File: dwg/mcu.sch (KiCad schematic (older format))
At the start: 3 parts

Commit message: updating board -- no DRC errors
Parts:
- added C17, C22, C23, C24, C25, C26, C27, C31: 0.1uF, Capacitors_SMD:C_0805_HandSoldering, symbol C_Small
- added C18, C20: 2.2uF, Capacitors_SMD:C_0805_HandSoldering, symbol C_Small
- added C19: 10uF, Capacitors_SMD:C_0805_HandSoldering, symbol C_Small
- added C28, C30: 20pF, Capacitors_SMD:C_0603_HandSoldering, symbol C_Small
- added C29: 1uF, Capacitors_SMD:C_0805_HandSoldering, symbol C_Small
- added J13: CONN_02X05, Connectors:IDC_Header_Straight_10pins, symbol CONN_02X05
- added R18, R19, R21: 10k, Resistors_SMD:R_0805_HandSoldering, symbol R_Small
- added R20: 300, Resistors_SMD:R_0603_HandSoldering, symbol R_Small
- added Y1: 8MHz, Crystals:Crystal_SMD_Abracon_ABM3-2pin_5.0x3.2mm_HandSoldering, symbol Crystal_Small
- SW1: renamed from SW?; value SW_PUSH -> TL3342; footprint (none) -> Buttons_Switches_SMD:SW_SPST_TL3342
- U3: renamed from U?; footprint LQFP100 -> Housings_QFP:LQFP-100_14x14mm_Pitch0.5mm
- gave numbers to parts that had none: 1
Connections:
- net CS_IRQ: now also U3.96 (CAN1_TX/DAC_EXTI9/DCMI_D7/I2C1_SDA/I2S2_WS/SDIO_D5/SPI2_NSS/TIM11_CH1/TIM4_CH4/PB9); no longer U3.1 (PE2/ETH_TXD3/FSMC_A23/SYS_TRACECLK)
- net GND: now also C21.2, U3.10 (VSS), U3.20 (VSSA), U3.27 (VSS), U3.74 (VSS), U3.99 (VSS), C17.2, C18.2, C19.2, C20.2, C22.2, C23.2, C24.2, C25.2, C26.2, C27.2, C29.2, C31.2, J13.3 (P3), J13.5 (P5), J13.9 (P9), R18.2, R19.2, R21.1; no longer C21.1
- net HAL_1: now also U3.78 (DCMI_D8/I2S3_CK/SDIO_D2/SPI3_SCK/UART4_TX/USART3_TX/PC10); no longer U3.5 (PE6/DCMI_D7/FSMC_A22/SYS_TRACED3/TIM9_CH2)
- net HAL_2: now also U3.82 (PD1/CAN1_TX/FSMC_D3/FSMC_DA3); no longer U3.3 (PE4/DCMI_D4/FSMC_A20/SYS_TRACED1)
- net VCC: now reaches U3.100 (VDD)
- net VCC: now also U3.11 (VDD), U3.19 (VDD), U3.28 (VDD), U3.50 (VDD), U3.6 (VBAT), U3.75 (VDD), C17.1, C19.1, C22.1, C23.1, C24.1, C25.1, C26.1, C27.1, J13.1 (P1)
- net OSC_IN: now reaches U3.12 (PH0/RCC_OSC_IN)
- net OSC_IN: now also C28.1, Y1.1
- net OSC_OUT: now reaches U3.13 (PH1/RCC_OSC_OUT)
- net OSC_OUT: now also R20.1
- net NRST: now reaches SW1.2, U3.14 (NRST)
- net NRST: now also C21.1, J13.10 (P10); no longer C21.2
- net VDDA: now reaches U3.21 (VREF+)
- net VDDA: now also U3.22 (VDDA), C29.1, C31.1
- net BOOT1: now reaches U3.37 (BOOT1/PB2)
- net BOOT1: now also R19.1
- net VCAP_1: now reaches U3.49 (VCAP_1)
- net VCAP_1: now also C20.1
- net JTMS/SWDIO: now reaches U3.72 (SYS_JTMS-SWDIO/PA13)
- net JTMS/SWDIO: now also J13.2 (P2)
- net VCAP_2: now reaches U3.73 (VCAP_2)
- net VCAP_2: now also C18.1
- net JTCK/SWCLK: now reaches U3.76 (SYS_JTCK-SWCLK/PA14)
- net JTCK/SWCLK: now also J13.4 (P4)
- net JTDI: now reaches U3.77 (ADC1_EXTI15/ADC2_EXTI15/ADC3_EXTI15/I2S3_WS/SPI1_NSS/SPI3_NSS/SYS_JTDI/TIM2_CH1/TIM2_ETR/PA15)
- net JTDI: now also J13.8 (P8)
- net JTDO/SWO: now reaches U3.89 (I2S3_CK/SPI1_SCK/SPI3_SCK/SYS_JTDO-SWO/TIM2_CH2/PB3)
- net JTDO/SWO: now also J13.6 (P6)
- net BOOT0: now reaches U3.94 (BOOT0)
- net BOOT0: now also R18.1
- new net: J13.7 (P7), R21.2
- new net: C30.1, R20.2, Y1.2
- new net: C28.2, C30.2
- no-connect marks 0 -> 53
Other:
- moved on the sheet: C21, SW1, U3

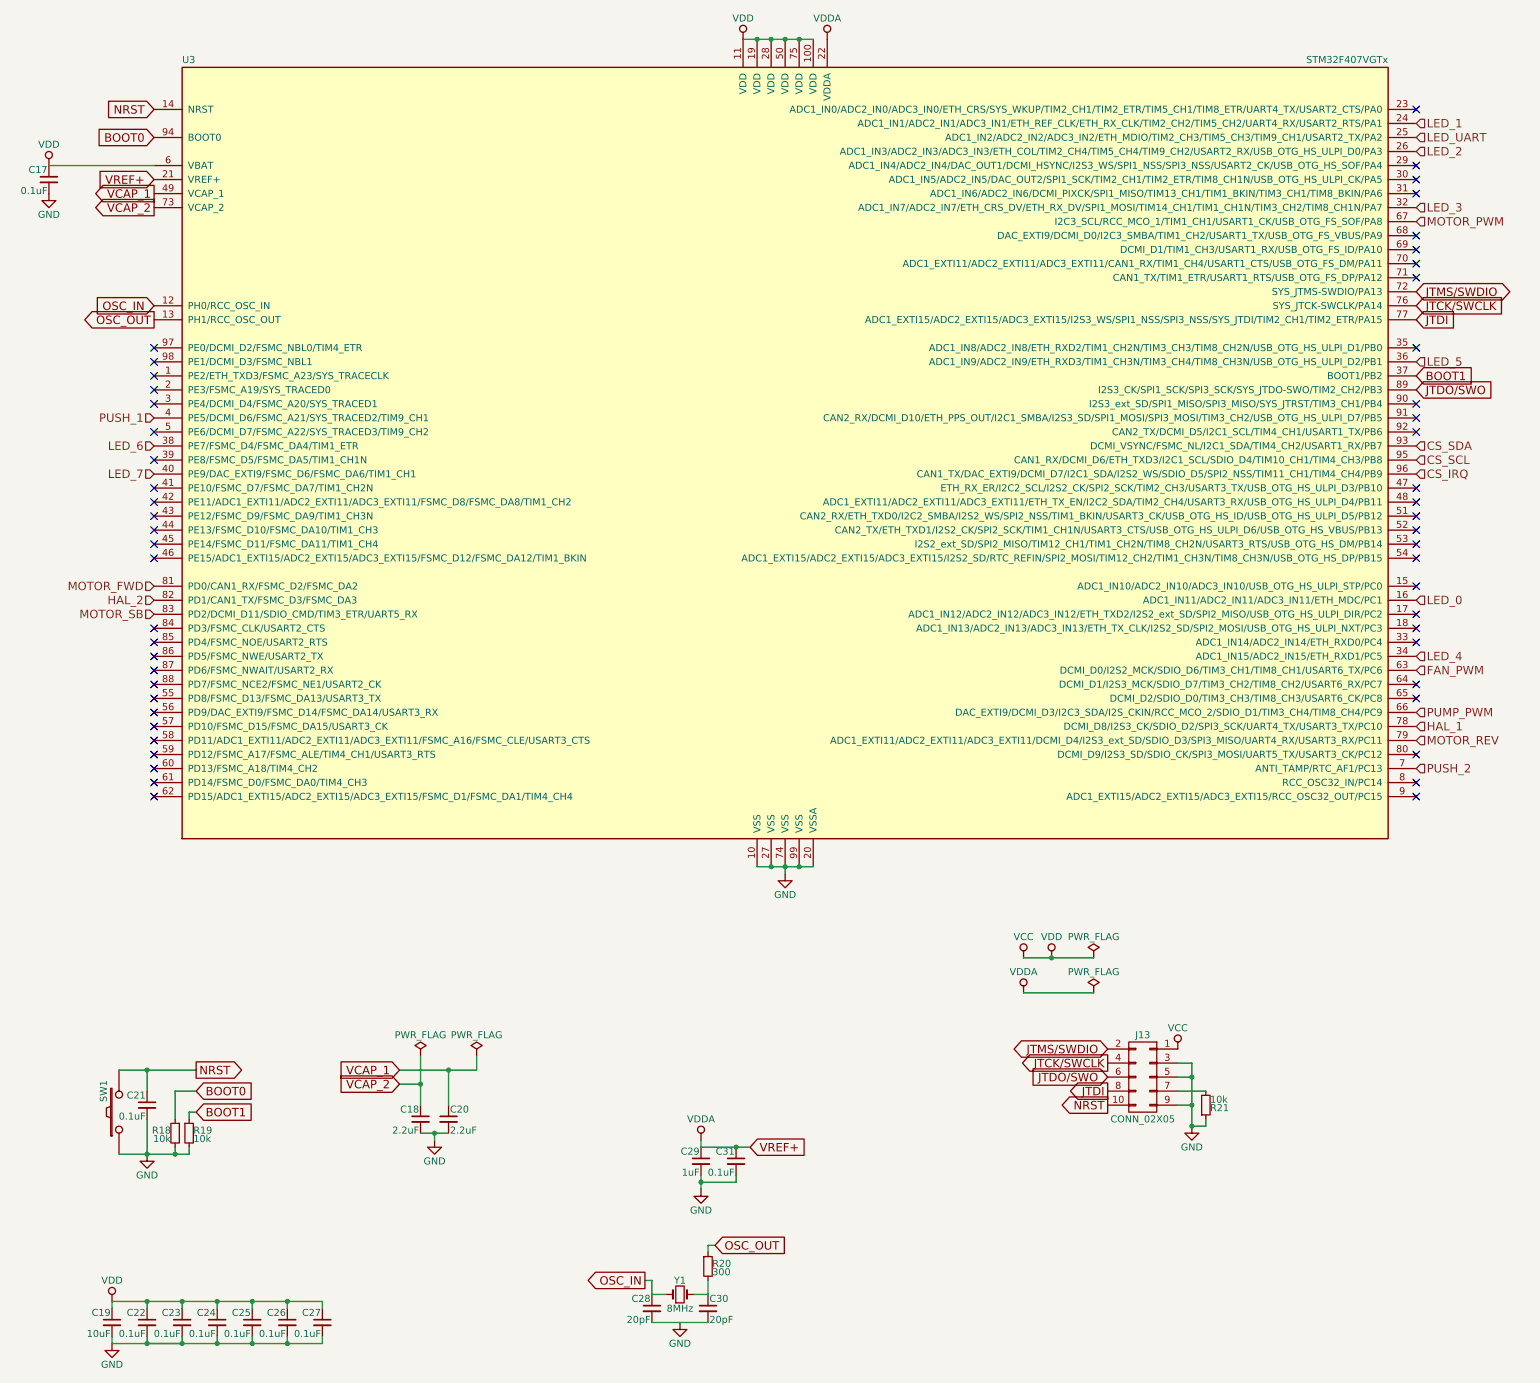
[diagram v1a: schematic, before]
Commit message: updated placement on new board. No DRC errors
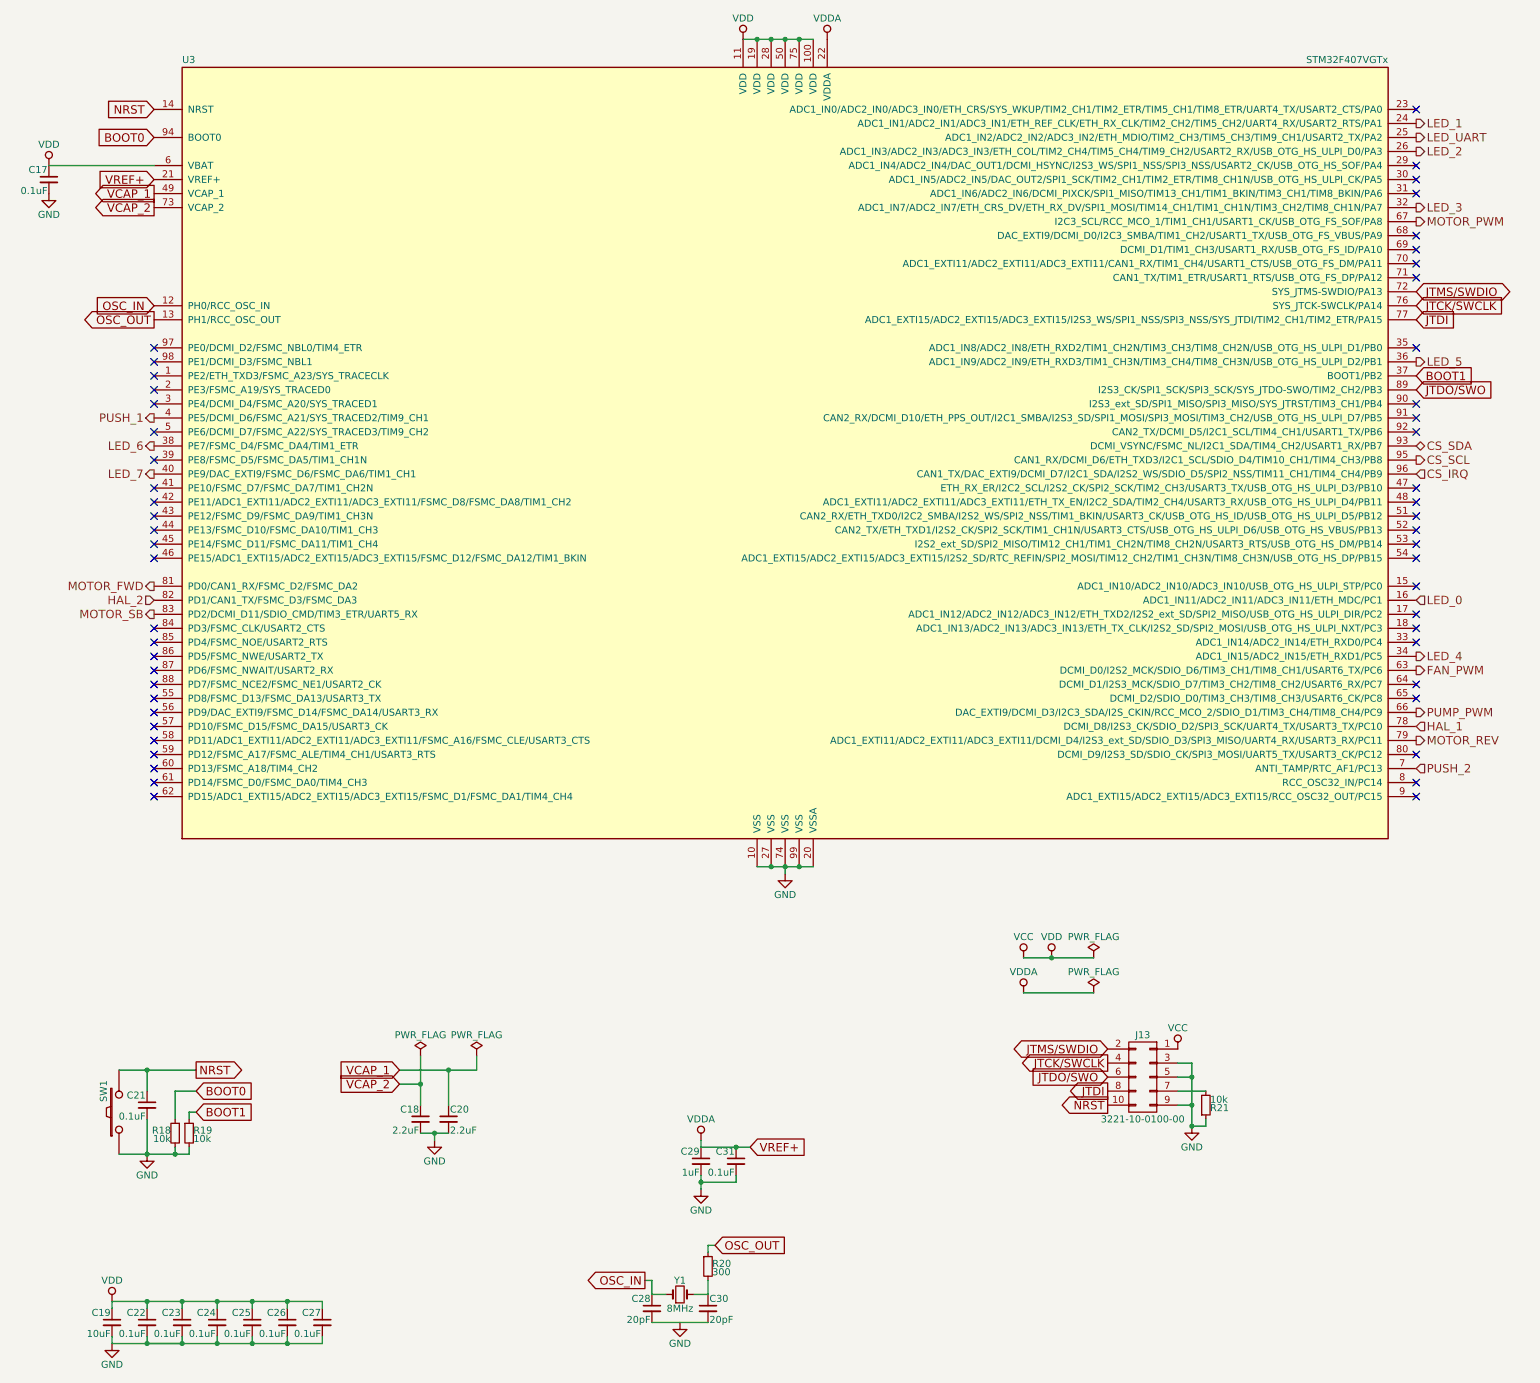
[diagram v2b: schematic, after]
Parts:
- C17, C18, C19, C20, C21, C22, C23, C24, C25, C26, C27, C29, C31: footprint Capacitors_SMD:C_0805_HandSoldering -> Capacitors_SMD:C_0603_HandSoldering
- J13: value CONN_02X05 -> 3221-10-0100-00; footprint Connectors:IDC_Header_Straight_10pins -> roboCooler:Header_02x05_50mil
- R18, R19, R21: footprint Resistors_SMD:R_0805_HandSoldering -> Resistors_SMD:R_0603_HandSoldering
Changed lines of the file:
@@
 Text HLabel 10450 4700 2    60   Input ~ 0
 LED_0
-Text HLabel 10450 1300 2    60   Input ~ 0
+Text HLabel 10450 1300 2    60   Output ~ 0
 LED_1
-Text HLabel 10450 1500 2    60   Input ~ 0
+Text HLabel 10450 1500 2    60   Output ~ 0
 LED_2
-Text HLabel 10450 1900 2    60   Input ~ 0
+Text HLabel 10450 1900 2    60   Output ~ 0
 LED_3
-Text HLabel 10450 5100 2    60   Input ~ 0
+Text HLabel 10450 5100 2    60   Output ~ 0
 LED_4
-Text HLabel 10450 3000 2    60   Input ~ 0
+Text HLabel 10450 3000 2    60   Output ~ 0
 LED_5
-Text HLabel 1450 3600 0    60   Input ~ 0
+Text HLabel 1450 3600 0    60   Output ~ 0
 LED_6
-Text HLabel 1450 3800 0    60   Input ~ 0
+Text HLabel 1450 3800 0    60   Output ~ 0
 LED_7
-Text HLabel 10450 1400 2    60   Input ~ 0
+Text HLabel 10450 1400 2    60   Output ~ 0
 LED_UART
 Text HLabel 10450 5600 2    60   Input ~ 0
@@
 Text HLabel 1450 4700 0    60   Input ~ 0
 HAL_2
-Text HLabel 1450 3400 0    60   Input ~ 0
+Text HLabel 1450 3400 0    60   Output ~ 0
 PUSH_1
 Text HLabel 10450 5900 2    60   Input ~ 0
@@
 Text HLabel 10450 3800 2    60   Input ~ 0
 CS_IRQ
-Text HLabel 10450 3700 2    60   Input ~ 0
+Text HLabel 10450 3700 2    60   Output ~ 0
 CS_SCL
-Text HLabel 10450 3600 2    60   Input ~ 0
+Text HLabel 10450 3600 2    60   BiDi ~ 0
 CS_SDA
-Text HLabel 1450 4800 0    60   Input ~ 0
+Text HLabel 1450 4800 0    60   Output ~ 0
 MOTOR_SB
-Text HLabel 1450 4600 0    60   Input ~ 0
+Text HLabel 1450 4600 0    60   Output ~ 0
 MOTOR_FWD
-Text HLabel 10450 5700 2    60   Input ~ 0
+Text HLabel 10450 5700 2    60   Output ~ 0
 MOTOR_REV
-Text HLabel 10450 2000 2    60   Input ~ 0
+Text HLabel 10450 2000 2    60   Output ~ 0
 MOTOR_PWM
-Text HLabel 10450 5200 2    60   Input ~ 0
+Text HLabel 10450 5200 2    60   Output ~ 0
 FAN_PWM
-Text HLabel 10450 5500 2    60   Input ~ 0
+Text HLabel 10450 5500 2    60   Output ~ 0
 PUMP_PWM
 $Comp
@@
 F 0 "C21" H 1410 8370 50  0000 L CNN
 F 1 "0.1uF" H 1410 8220 50  0000 L CNN
-F 2 "Capacitors_SMD:C_0805_HandSoldering" H 1400 8300 50  0001 C CNN
+F 2 "Capacitors_SMD:C_0603_HandSoldering" H 1400 8300 50  0001 C CNN
 F 3 "" H 1400 8300 50  0001 C CNN
 	1    1400 8300
@@
 F 0 "R19" H 1730 8520 50  0000 L CNN
 F 1 "10k" H 1730 8460 50  0000 L CNN
-F 2 "Resistors_SMD:R_0805_HandSoldering" H 1700 8500 50  0001 C CNN
+F 2 "Resistors_SMD:R_0603_HandSoldering" H 1700 8500 50  0001 C CNN
 F 3 "" H 1700 8500 50  0001 C CNN
 	1    1700 8500
@@
 F 0 "R18" H 1630 8520 50  0000 L CNN
 F 1 "10k" H 1630 8460 50  0000 L CNN
-F 2 "Resistors_SMD:R_0805_HandSoldering" H 1600 8500 50  0001 C CNN
+F 2 "Resistors_SMD:R_0603_HandSoldering" H 1600 8500 50  0001 C CNN
 F 3 "" H 1600 8500 50  0001 C CNN
 	1    1600 8500
@@
 F 0 "C19" H 1160 9920 50  0000 L CNN
 F 1 "10uF" H 1160 9770 50  0000 L CNN
-F 2 "Capacitors_SMD:C_0805_HandSoldering" H 1150 9850 50  0001 C CNN
+F 2 "Capacitors_SMD:C_0603_HandSoldering" H 1150 9850 50  0001 C CNN
 F 3 "" H 1150 9850 50  0001 C CNN
 	1    1150 9850
@@
 F 0 "C22" H 1410 9920 50  0000 L CNN
 F 1 "0.1uF" H 1410 9770 50  0000 L CNN
-F 2 "Capacitors_SMD:C_0805_HandSoldering" H 1400 9850 50  0001 C CNN
+F 2 "Capacitors_SMD:C_0603_HandSoldering" H 1400 9850 50  0001 C CNN
 F 3 "" H 1400 9850 50  0001 C CNN
 	1    1400 9850
@@
 F 0 "C23" H 1660 9920 50  0000 L CNN
 F 1 "0.1uF" H 1660 9770 50  0000 L CNN
-F 2 "Capacitors_SMD:C_0805_HandSoldering" H 1650 9850 50  0001 C CNN
+F 2 "Capacitors_SMD:C_0603_HandSoldering" H 1650 9850 50  0001 C CNN
 F 3 "" H 1650 9850 50  0001 C CNN
 	1    1650 9850
@@
 F 0 "C24" H 1910 9920 50  0000 L CNN
 F 1 "0.1uF" H 1910 9770 50  0000 L CNN
-F 2 "Capacitors_SMD:C_0805_HandSoldering" H 1900 9850 50  0001 C CNN
+F 2 "Capacitors_SMD:C_0603_HandSoldering" H 1900 9850 50  0001 C CNN
 F 3 "" H 1900 9850 50  0001 C CNN
 	1    1900 9850
@@
 F 0 "C25" H 2160 9920 50  0000 L CNN
 F 1 "0.1uF" H 2160 9770 50  0000 L CNN
-F 2 "Capacitors_SMD:C_0805_HandSoldering" H 2150 9850 50  0001 C CNN
+F 2 "Capacitors_SMD:C_0603_HandSoldering" H 2150 9850 50  0001 C CNN
 F 3 "" H 2150 9850 50  0001 C CNN
 	1    2150 9850
@@
 F 0 "C26" H 2410 9920 50  0000 L CNN
 F 1 "0.1uF" H 2410 9770 50  0000 L CNN
-F 2 "Capacitors_SMD:C_0805_HandSoldering" H 2400 9850 50  0001 C CNN
+F 2 "Capacitors_SMD:C_0603_HandSoldering" H 2400 9850 50  0001 C CNN
 F 3 "" H 2400 9850 50  0001 C CNN
 	1    2400 9850
@@
 F 0 "C27" H 2660 9920 50  0000 L CNN
 F 1 "0.1uF" H 2660 9770 50  0000 L CNN
-F 2 "Capacitors_SMD:C_0805_HandSoldering" H 2650 9850 50  0001 C CNN
+F 2 "Capacitors_SMD:C_0603_HandSoldering" H 2650 9850 50  0001 C CNN
 F 3 "" H 2650 9850 50  0001 C CNN
 	1    2650 9850
@@
 F 0 "C17" H 710 1770 50  0000 L CNN
 F 1 "0.1uF" H 710 1620 50  0000 L CNN
-F 2 "Capacitors_SMD:C_0805_HandSoldering" H 700 1700 50  0001 C CNN
+F 2 "Capacitors_SMD:C_0603_HandSoldering" H 700 1700 50  0001 C CNN
 F 3 "" H 700 1700 50  0001 C CNN
 	1    700  1700
@@
 F 0 "C29" H 5360 8770 50  0000 L CNN
 F 1 "1uF" H 5360 8620 50  0000 L CNN
-F 2 "Capacitors_SMD:C_0805_HandSoldering" H 5350 8700 50  0001 C CNN
+F 2 "Capacitors_SMD:C_0603_HandSoldering" H 5350 8700 50  0001 C CNN
 F 3 "" H 5350 8700 50  0001 C CNN
 	1    5350 8700
@@
 F 0 "C31" H 5610 8770 50  0000 L CNN
 F 1 "0.1uF" H 5610 8620 50  0000 L CNN
-F 2 "Capacitors_SMD:C_0805_HandSoldering" H 5600 8700 50  0001 C CNN
+F 2 "Capacitors_SMD:C_0603_HandSoldering" H 5600 8700 50  0001 C CNN
 F 3 "" H 5600 8700 50  0001 C CNN
 	1    5600 8700
@@
 F 0 "C18" H 3360 8470 50  0000 L CNN
 F 1 "2.2uF" H 3360 8320 50  0000 L CNN
-F 2 "Capacitors_SMD:C_0805_HandSoldering" H 3350 8400 50  0001 C CNN
+F 2 "Capacitors_SMD:C_0603_HandSoldering" H 3350 8400 50  0001 C CNN
 F 3 "" H 3350 8400 50  0001 C CNN
 	1    3350 8400
@@
 F 0 "C20" H 3560 8470 50  0000 L CNN
 F 1 "2.2uF" H 3560 8320 50  0000 L CNN
-F 2 "Capacitors_SMD:C_0805_HandSoldering" H 3550 8400 50  0001 C CNN
+F 2 "Capacitors_SMD:C_0603_HandSoldering" H 3550 8400 50  0001 C CNN
 F 3 "" H 3550 8400 50  0001 C CNN
 	1    3550 8400
@@
 F 0 "R21" H 8980 8320 50  0000 L CNN
 F 1 "10k" H 8980 8260 50  0000 L CNN
-F 2 "Resistors_SMD:R_0805_HandSoldering" H 8950 8300 50  0001 C CNN
+F 2 "Resistors_SMD:R_0603_HandSoldering" H 8950 8300 50  0001 C CNN
 F 3 "" H 8950 8300 50  0001 C CNN
 	1    8950 8300
@@
 P 8500 8100
 F 0 "J13" H 8500 8400 50  0000 C CNN
-F 1 "CONN_02X05" H 8500 7800 50  0000 C CNN
-F 2 "Connectors:IDC_Header_Straight_10pins" H 8500 6900 50  0001 C CNN
-F 3 "" H 8500 6900 50  0001 C CNN
+F 1 "3221-10-0100-00" H 8500 7800 50  0000 C CNN
+F 2 "roboCooler:Header_02x05_50mil" H 8500 6900 50  0001 C CNN
+F 3 "http://cnctech.us/pdfs/3221-XX-0100-00.pdf" H 8500 6900 50  0001 C CNN
 	1    8500 8100
 	-1   0    0    -1
